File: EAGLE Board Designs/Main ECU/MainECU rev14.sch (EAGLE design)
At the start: 325 parts, among them J1 CONNECTOR-34__, J2 CONNECTOR-34__, J3 ADIS16460, K1 RELAY_DPDT_07DSMT, K2 RELAY_DPDT_07DSMT, K3 RELAY_DPDT_07DSMT, K4 RELAY_DPDT_07DSMT, K5 RELAY_DPDT_07DSMT, Q1 TRANSISTOR_N_MOS__DMG3406L-7, Q2 TRANSISTOR_P_MOS_SOT-23_DMP30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, Q3 TRANSISTOR_P_MOS_SOT-23_DMP30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, Q4 TRANSISTOR_N_MOS__DMG3406L-7, U1 MAX7400, U10 MCP3208, U11 MCP3208, U12 TCAN1051HQV-Q1, U13 TCAN1051HQV-Q1, U15 OPAMP_1_CHANNEL_OPA991, U16 LOGICGATE_OR, U17 OPAMP_1_CHANNEL_OPA991, U18 LOGICGATE_OR, U19 OPAMP_1_CHANNEL_OPA991, U2 MAX7400, U20 LOGICGATE_OR, U21 LOGICGATE_OR, U22 OPAMP_1_CHANNEL_OPA991, U23 LOGICGATE_NOR, U24 LOGICGATE_OR, U25 OPAMP_1_CHANNEL_OPA991, U26 OPAMP_1_CHANNEL_OPA991, U27 OPAMP_1_CHANNEL_OPA991, U28 LOGICGATE_AND_DCK3, U29 OPAMP_1_CHANNEL_OPA991, U3 MAX7400, U30 OPAMP_1_CHANNEL_OPA991, U31 TCAN1051HQV-Q1, U32 TCAN1051HQV-Q1, U33 TCAN1051HQV-Q1, U34 TCAN1051HQV-Q1, U35 MAX7400, U36 MAX7400, U37 ADM8316WBX30, U38 MAX7400, U4 MAX7400, U5 VOLTAGE_REGULATOR_SOT-223_3.3V, U6 MAX7400, U7 MAX7400, U8 MAX7400, U9 MAX7400

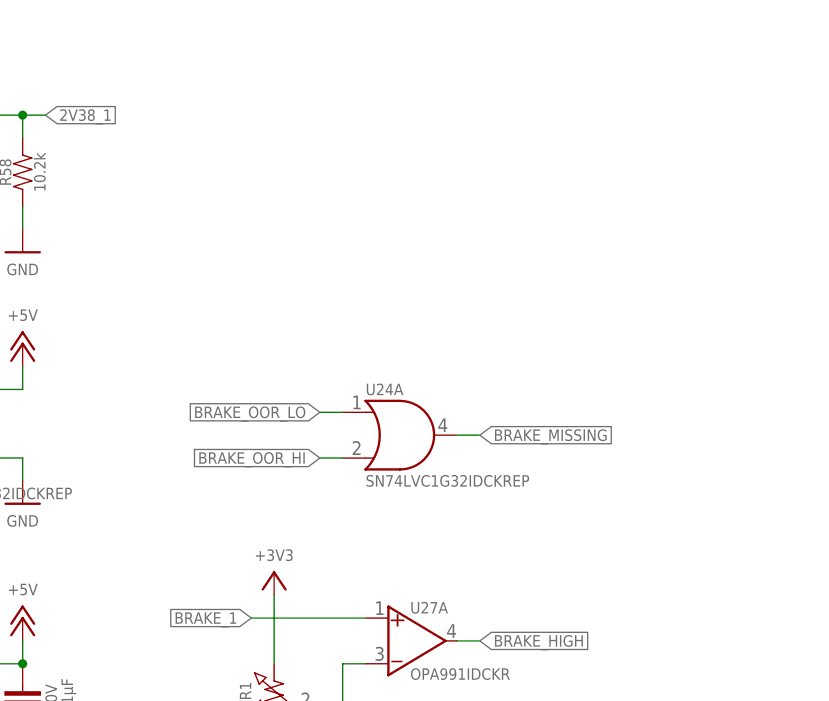
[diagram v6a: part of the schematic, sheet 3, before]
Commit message: added selectable reference pot
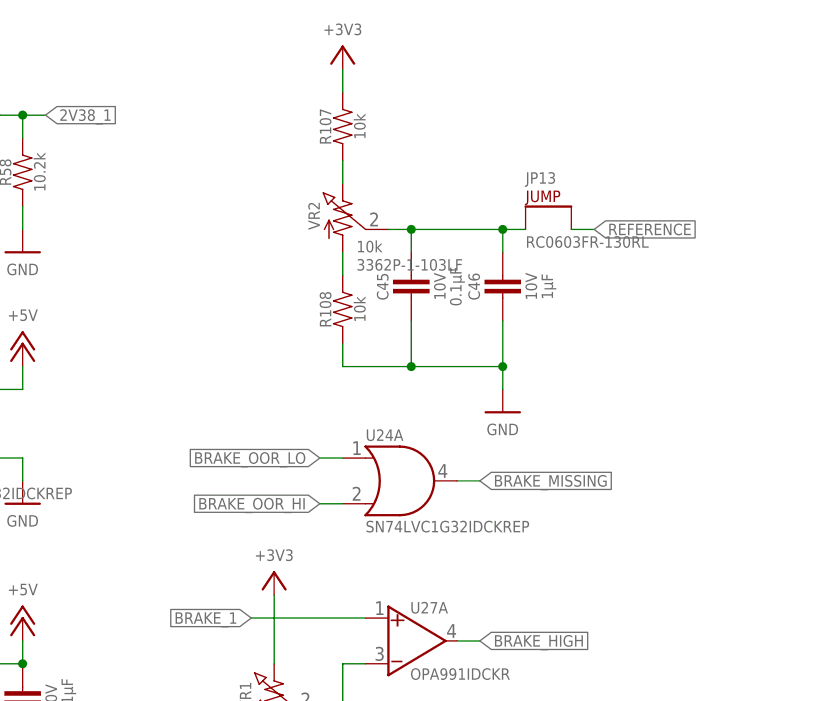
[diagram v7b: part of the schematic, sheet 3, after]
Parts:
- added C45: CAPACITOR_0603_10V_0.1UF, HyTechDevices:CAPACITOR_0603_10V_0.1UF
- added C46: CAPACITOR_0603_10V_1UF, HyTechDevices:CAPACITOR_0603_10V_1UF
- added JP12: JUMPER_0603_, HyTechDevices:JUMPER_0603_
- added JP13: DNP, HyTechDevices:JUMPER_0603_
- added R107, R108: RESISTOR_0603_10K, HyTechDevices:RESISTOR_0603_10K
- added VR2: RESISTOR_TRIMPOT_10K_3362P, HyTechDevices:RESISTOR_TRIMPOT_10K_3362P
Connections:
- new net N$34: JP12.2, U9.OUT
- new net N$39: R107.1, VR2.2
- new net N$46: C45.1, C46.1, JP13.1, VR2.3
- new net N$48: R108.2, VR2.1
- net +3V3: now also R107.2
- net GND: now also C45.2, C46.2, R108.1
- net REFERENCE: now also JP12.1, JP13.2; no longer U9.OUT
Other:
- moved on the sheet: TP10, U24A
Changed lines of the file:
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@@
 <part name="D27" library="HyTechDevices" deviceset="TVS_?_*" device="DO-214AA" technology="28V" value="TVS_DO-214AA_28V"/>
 <part name="P63" library="HyTechSupplies" deviceset="GND" device=""/>
+<part name="JP12" library="HyTechDevices" deviceset="JUMPER_?_*" device="0603"/>
+<part name="VR2" library="HyTechDevices" deviceset="RESISTOR_TRIMPOT_*_?" device="3362P" technology="10K"/>
+<part name="P89" library="HyTechSupplies" deviceset="+3V3" device=""/>
+<part name="P90" library="HyTechSupplies" deviceset="GND" device=""/>
+<part name="C45" library="HyTechDevices" deviceset="CAPACITOR_?_*" device="0603" technology="10V_0.1UF"/>
+<part name="C46" library="HyTechDevices" deviceset="CAPACITOR_?_*" device="0603" technology="10V_1UF"/>
+<part name="JP13" library="HyTechDevices" deviceset="JUMPER_?_*" device="0603" value="DNP"/>
+<part name="R107" library="HyTechDevices" deviceset="RESISTOR_?_*" device="0603" technology="10K"/>
+<part name="R108" library="HyTechDevices" deviceset="RESISTOR_?_*" device="0603" technology="10K"/>
 </parts>
 <sheets>
@@
 <attribute name="MPN" x="147.32" y="151.638" size="1.27" layer="95" rot="R180" align="top-left"/>
 </instance>
-<instance part="U24" gate="A" x="228.6" y="165.1" smashed="yes">
-<attribute name="NAME" x="228.6" y="169.545" size="1.27" layer="95"/>
-<attribute name="MPN" x="228.6" y="160.655" size="1.27" layer="96" align="top-left"/>
+<instance part="U24" gate="A" x="228.6" y="160.02" smashed="yes">
+<attribute name="NAME" x="228.6" y="164.465" size="1.27" layer="95"/>
+<attribute name="MPN" x="228.6" y="155.575" size="1.27" layer="96" align="top-left"/>
 </instance>
 <instance part="U24" gate="P" x="177.8" y="172.72" smashed="yes">
@@
 <attribute name="VALUE" x="88.9" y="67.31" size="1.27" layer="96" align="bottom-center"/>
 </instance>
+<instance part="VR2" gate="G$1" x="226.06" y="190.5" smashed="yes">
+<attribute name="NAME" x="223.52" y="189.484" size="1.27" layer="95" rot="R90" align="bottom-center"/>
+<attribute name="RESISTANCE" x="227.584" y="186.69" size="1.27" layer="96" align="top-left"/>
+<attribute name="MPN" x="227.584" y="184.658" size="1.27" layer="96" align="top-left"/>
+</instance>
+<instance part="P89" gate="G$1" x="226.06" y="208.28" smashed="yes">
+<attribute name="VALUE" x="226.06" y="209.55" size="1.27" layer="96" align="bottom-center"/>
+</instance>
+<instance part="P90" gate="1" x="243.84" y="167.64" smashed="yes">
+<attribute name="VALUE" x="243.84" y="166.37" size="1.27" layer="96" align="top-center"/>
+</instance>
+<instance part="C45" gate="G$1" x="233.68" y="182.88" smashed="yes" rot="R90">
+<attribute name="NAME" x="231.14" y="181.61" size="1.27" layer="95" rot="R90" align="bottom-center"/>
+<attribute name="VOLTAGE" x="236.22" y="181.61" size="1.27" layer="96" rot="R90" align="top-center"/>
+<attribute name="CAPACITANCE" x="237.998" y="181.61" size="1.27" layer="96" rot="R90" align="top-center"/>
+</instance>
+<instance part="C46" gate="G$1" x="243.84" y="182.88" smashed="yes" rot="R90">
+<attribute name="NAME" x="241.3" y="181.61" size="1.27" layer="95" rot="R90" align="bottom-center"/>
+<attribute name="VOLTAGE" x="246.38" y="181.61" size="1.27" layer="96" rot="R90" align="top-center"/>
+<attribute name="CAPACITANCE" x="248.158" y="181.61" size="1.27" layer="96" rot="R90" align="top-center"/>
+</instance>
+<instance part="JP13" gate="G$1" x="246.38" y="190.5" smashed="yes">
+<attribute name="NAME" x="246.38" y="193.04" size="1.27" layer="95"/>
+<attribute name="MPN" x="246.38" y="187.198" size="1.27" layer="96" align="top-left"/>
+</instance>
+<instance part="R107" gate="G$1" x="226.06" y="200.66" smashed="yes" rot="R90">
+<attribute name="NAME" x="224.79" y="199.39" size="1.27" layer="95" rot="R90" align="bottom-center"/>
+<attribute name="RESISTANCE" x="227.33" y="199.39" size="1.27" layer="96" rot="R90" align="top-center"/>
+</instance>
+<instance part="R108" gate="G$1" x="226.06" y="180.34" smashed="yes" rot="R90">
+<attribute name="NAME" x="224.79" y="179.07" size="1.27" layer="95" rot="R90" align="bottom-center"/>
+<attribute name="RESISTANCE" x="227.33" y="179.07" size="1.27" layer="96" rot="R90" align="top-center"/>
+</instance>
 </instances>
 <busses>
@@
 <wire x1="190.5" y1="190.5" x2="190.5" y2="187.96" width="0.1524" layer="91"/>
 </segment>
+<segment>
+<wire x1="226.06" y1="172.72" x2="233.68" y2="172.72" width="0.1524" layer="91"/>
+<pinref part="C46" gate="G$1" pin="2"/>
+<wire x1="233.68" y1="172.72" x2="243.84" y2="172.72" width="0.1524" layer="91"/>
+<wire x1="243.84" y1="172.72" x2="243.84" y2="177.8" width="0.1524" layer="91"/>
+<pinref part="P90" gate="1" pin="GND"/>
+<wire x1="243.84" y1="172.72" x2="243.84" y2="170.18" width="0.1524" layer="91"/>
+<junction x="243.84" y="172.72"/>
+<pinref part="C45" gate="G$1" pin="2"/>
+<wire x1="233.68" y1="177.8" x2="233.68" y2="172.72" width="0.1524" layer="91"/>
+<junction x="233.68" y="172.72"/>
+<pinref part="R108" gate="G$1" pin="1"/>
+<wire x1="226.06" y1="175.26" x2="226.06" y2="172.72" width="0.1524" layer="91"/>
+</segment>
 </net>
 <net name="N$67" class="0">
@@
 <label x="106.68" y="205.74" size="1.27" layer="95" rot="R180" xref="yes"/>
 </segment>
+<segment>
+<pinref part="JP13" gate="G$1" pin="2"/>
+<wire x1="251.46" y1="187.96" x2="254" y2="187.96" width="0.1524" layer="91"/>
+<label x="254" y="187.96" size="1.27" layer="95" xref="yes"/>
+</segment>
 </net>
 <net name="N$65" class="0">
@@
 <segment>
 <pinref part="U24" gate="A" pin="OUT"/>
-<wire x1="238.76" y1="165.1" x2="241.3" y2="165.1" width="0.1524" layer="91"/>
-<label x="241.3" y="165.1" size="1.27" layer="95" xref="yes"/>
+<wire x1="238.76" y1="160.02" x2="241.3" y2="160.02" width="0.1524" layer="91"/>
+<label x="241.3" y="160.02" size="1.27" layer="95" xref="yes"/>
 </segment>
 </net>
@@
 </segment>
 <segment>
-<wire x1="226.06" y1="162.56" x2="223.52" y2="162.56" width="0.1524" layer="91"/>
-<label x="223.52" y="162.56" size="1.27" layer="95" rot="R180" xref="yes"/>
+<wire x1="226.06" y1="157.48" x2="223.52" y2="157.48" width="0.1524" layer="91"/>
+<label x="223.52" y="157.48" size="1.27" layer="95" rot="R180" xref="yes"/>
 <pinref part="U24" gate="A" pin="IN2"/>
 </segment>
@@
 </segment>
 <segment>
-<wire x1="226.06" y1="167.64" x2="223.52" y2="167.64" width="0.1524" layer="91"/>
-<label x="223.52" y="167.64" size="1.27" layer="95" rot="R180" xref="yes"/>
+<wire x1="226.06" y1="162.56" x2="223.52" y2="162.56" width="0.1524" layer="91"/>
+<label x="223.52" y="162.56" size="1.27" layer="95" rot="R180" xref="yes"/>
 <pinref part="U24" gate="A" pin="IN1"/>
 </segment>
@@
 <pinref part="P58" gate="G$1" pin="+3V3"/>
 </segment>
+<segment>
+<pinref part="P89" gate="G$1" pin="+3V3"/>
+<pinref part="R107" gate="G$1" pin="2"/>
+<wire x1="226.06" y1="205.74" x2="226.06" y2="203.2" width="0.1524" layer="91"/>
+</segment>
 </net>
 <net name="2V38_1" class="0">
@@
 </segment>
 </net>
+<net name="N$46" class="0">
+<segment>
+<pinref part="VR2" gate="G$1" pin="3"/>
+<wire x1="231.14" y1="187.96" x2="233.68" y2="187.96" width="0.1524" layer="91"/>
+<pinref part="C46" gate="G$1" pin="1"/>
+<wire x1="233.68" y1="187.96" x2="243.84" y2="187.96" width="0.1524" layer="91"/>
+<wire x1="243.84" y1="187.96" x2="246.38" y2="187.96" width="0.1524" layer="91"/>
+<wire x1="243.84" y1="185.42" x2="243.84" y2="187.96" width="0.1524" layer="91"/>
+<junction x="243.84" y="187.96"/>
+<pinref part="C45" gate="G$1" pin="1"/>
+<wire x1="233.68" y1="185.42" x2="233.68" y2="187.96" width="0.1524" layer="91"/>
+<junction x="233.68" y="187.96"/>
+<pinref part="JP13" gate="G$1" pin="1"/>
+</segment>
+</net>
+<net name="N$39" class="0">
+<segment>
+<pinref part="R107" gate="G$1" pin="1"/>
+<pinref part="VR2" gate="G$1" pin="2"/>
+<wire x1="226.06" y1="195.58" x2="226.06" y2="193.04" width="0.1524" layer="91"/>
+</segment>
+</net>
+<net name="N$48" class="0">
+<segment>
+<pinref part="VR2" gate="G$1" pin="1"/>
+<pinref part="R108" gate="G$1" pin="2"/>
+<wire x1="226.06" y1="185.42" x2="226.06" y2="182.88" width="0.1524" layer="91"/>
+</segment>
+</net>
 </nets>
 </sheet>
@@
 <attribute name="MPN" x="99.06" y="187.198" size="1.27" layer="95" rot="R180" align="top-left"/>
 </instance>
-<instance part="TP10" gate="G$1" x="96.52" y="157.48" smashed="yes" rot="R180">
-<attribute name="NAME" x="99.06" y="155.702" size="1.27" layer="95" rot="R180"/>
-<attribute name="MPN" x="99.06" y="159.258" size="1.27" layer="95" rot="R180" align="top-left"/>
+<instance part="TP10" gate="G$1" x="101.6" y="157.48" smashed="yes" rot="R180">
+<attribute name="NAME" x="104.14" y="155.702" size="1.27" layer="95" rot="R180"/>
+<attribute name="MPN" x="104.14" y="159.258" size="1.27" layer="95" rot="R180" align="top-left"/>
+</instance>
+<instance part="JP12" gate="G$1" x="96.52" y="154.94" smashed="yes" rot="R180">
+<attribute name="NAME" x="96.52" y="152.4" size="1.27" layer="95" rot="R180"/>
+<attribute name="MPN" x="96.52" y="148.082" size="1.27" layer="96" rot="R180" align="top-left"/>
 </instance>
 </instances>
@@
 </segment>
 </net>
-<net name="REFERENCE" class="0">
-<segment>
-<pinref part="U9" gate="G$1" pin="OUT"/>
-<label x="91.44" y="157.48" size="1.27" layer="95" xref="yes"/>
-<pinref part="TP10" gate="G$1" pin="1"/>
-<wire x1="93.98" y1="157.48" x2="88.9" y2="157.48" width="0.1524" layer="91"/>
-</segment>
-</net>
 <net name="N$57" class="0">
 <segment>
@@
 </segment>
 </net>
+<net name="N$34" class="0">
+<segment>
+<pinref part="U9" gate="G$1" pin="OUT"/>
+<pinref part="JP12" gate="G$1" pin="2"/>
+<wire x1="88.9" y1="157.48" x2="91.44" y2="157.48" width="0.1524" layer="91"/>
+</segment>
+</net>
+<net name="REFERENCE" class="0">
+<segment>
+<pinref part="JP12" gate="G$1" pin="1"/>
+<pinref part="TP10" gate="G$1" pin="1"/>
+<wire x1="96.52" y1="157.48" x2="99.06" y2="157.48" width="0.1524" layer="91"/>
+<label x="88.9" y="157.48" size="1.27" layer="95"/>
+</segment>
+</net>

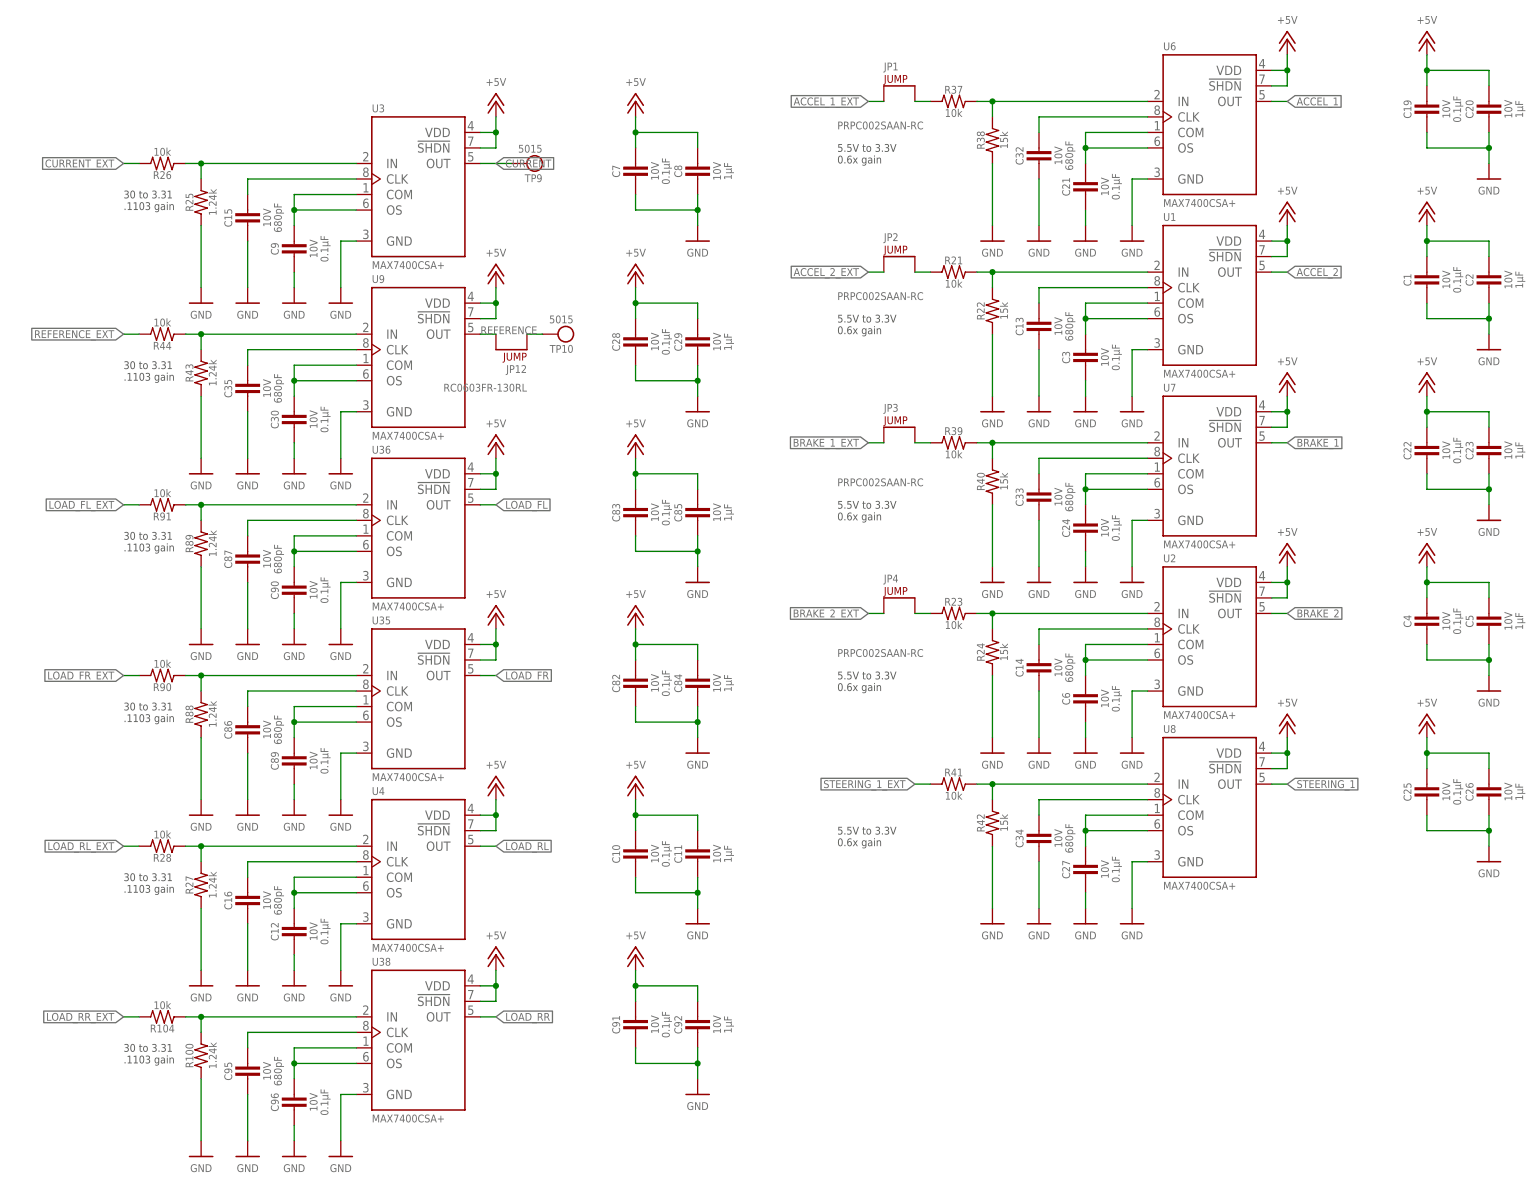
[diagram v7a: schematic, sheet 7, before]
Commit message: lowered corner frequency on filters to 50hz
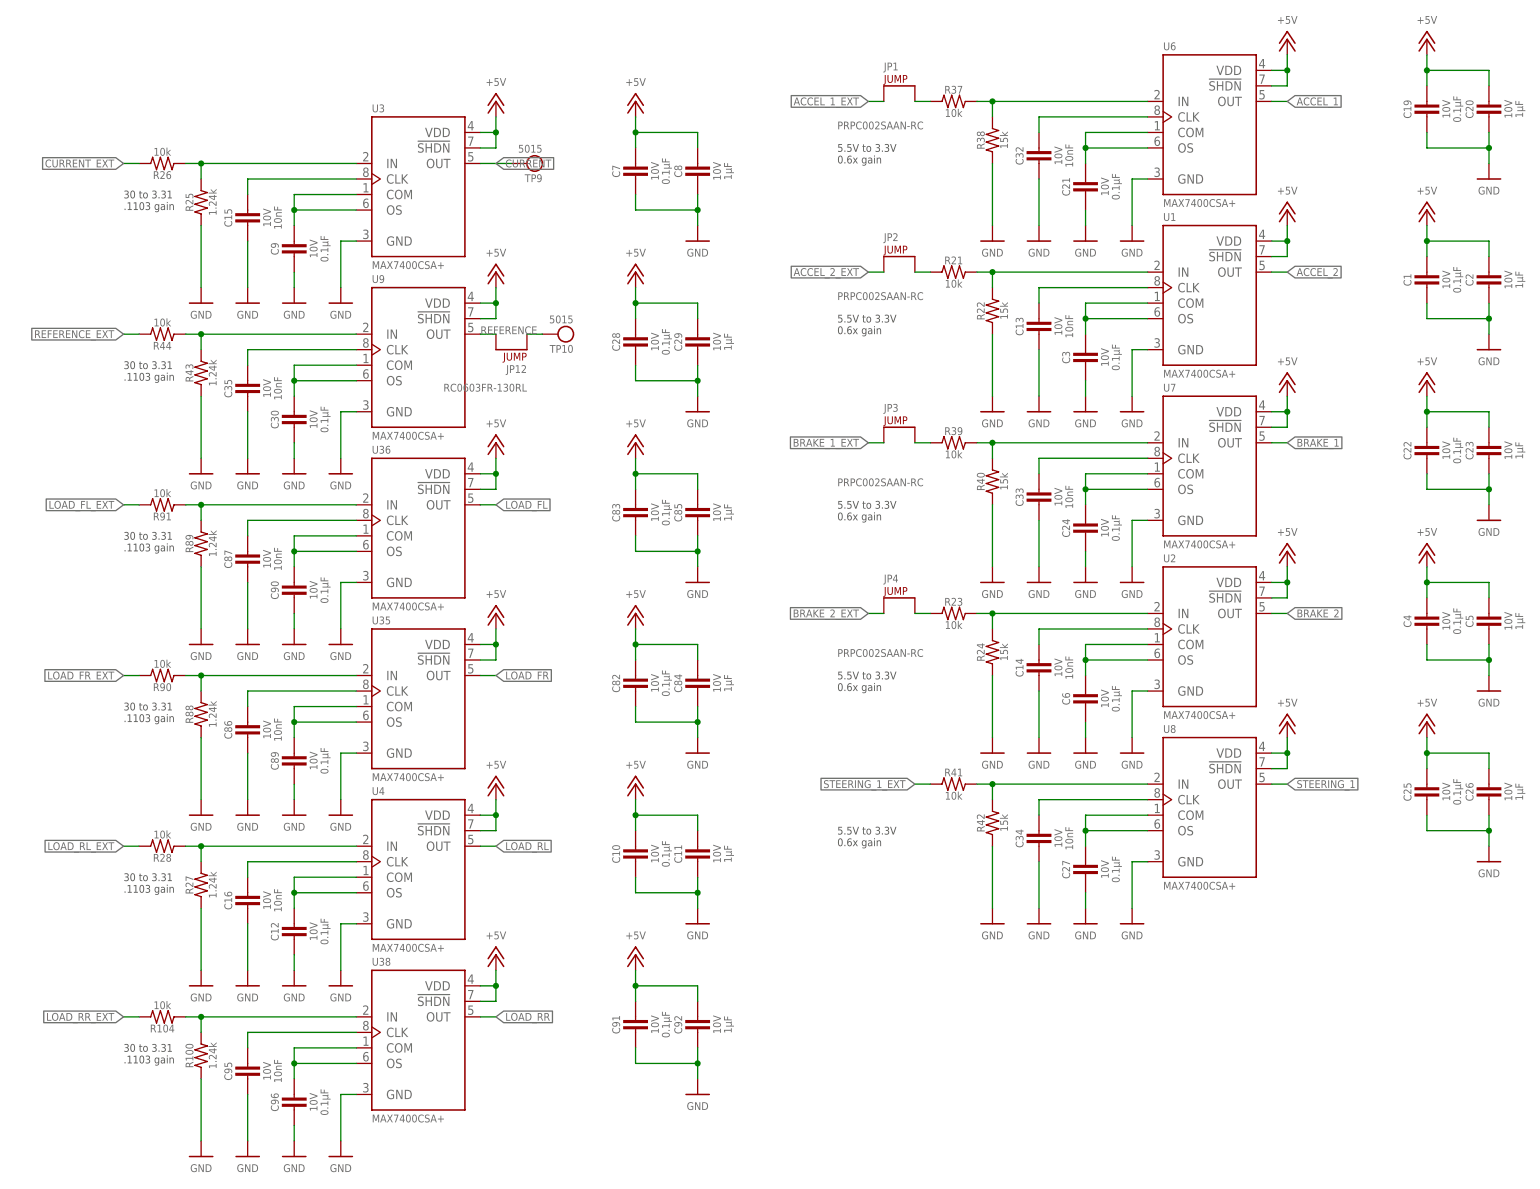
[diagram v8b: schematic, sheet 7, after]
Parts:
- C13, C14, C15, C16, C32, C33, C34, C35, C86, C87, C95: value CAPACITOR_0603_10V_680PF -> CAPACITOR_0603_10V_10NF; device HyTechDevices:CAPACITOR_0603_10V_680PF -> HyTechDevices:CAPACITOR_0603_10V_10NF
- C72, C73, C74, C75, C77, C78, C93, C94: value CAPACITOR_0603_10V_680PF -> CAPACITOR_0603_10V_0.1UF; device HyTechDevices:CAPACITOR_0603_10V_680PF -> HyTechDevices:CAPACITOR_0603_10V_0.1UF
